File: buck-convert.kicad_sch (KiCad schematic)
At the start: 11 parts, among them IC1 LMR36510FADDAR

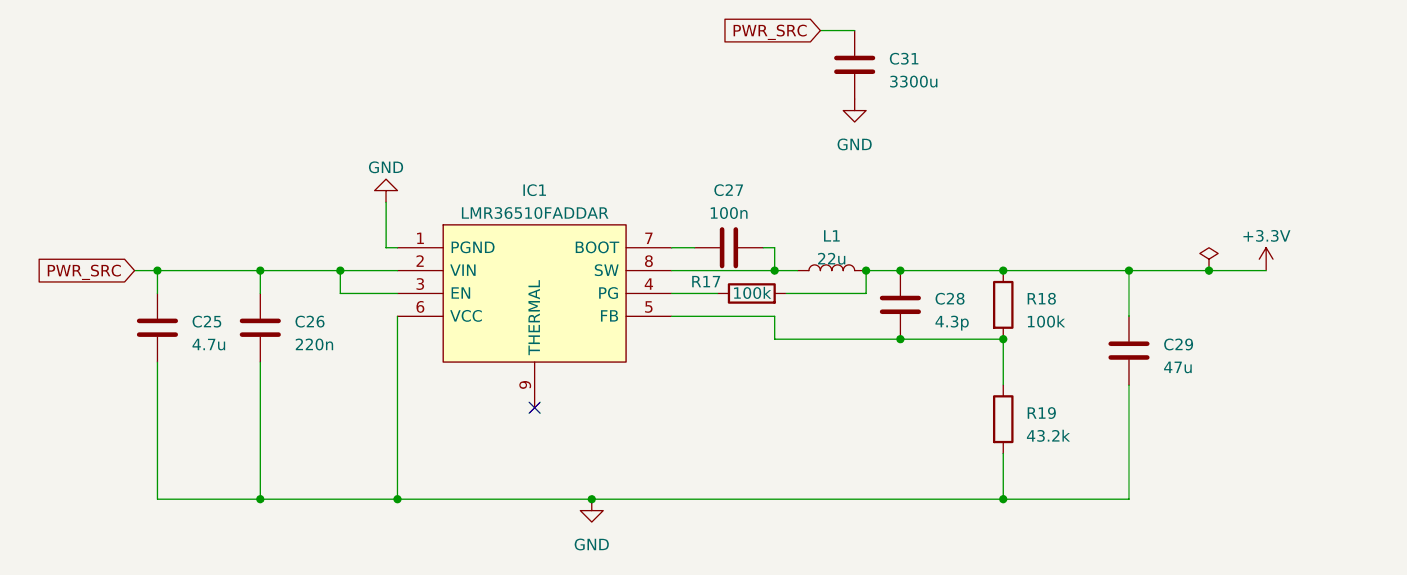
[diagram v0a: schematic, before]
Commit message: added nets to high level circuit
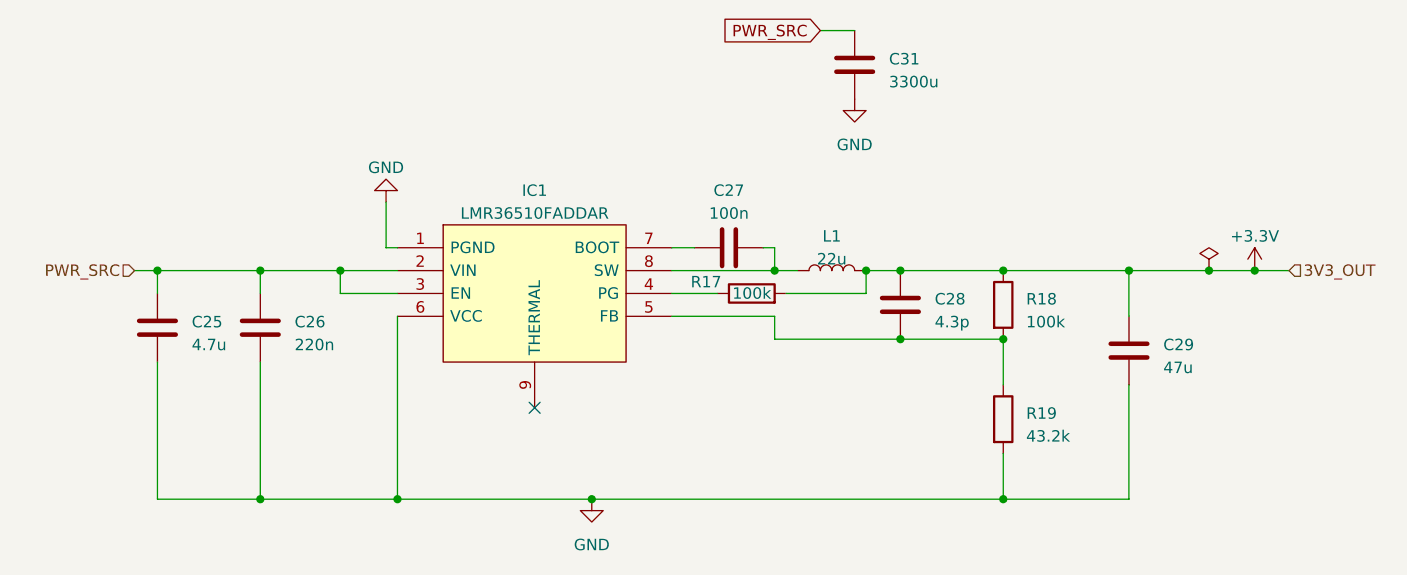
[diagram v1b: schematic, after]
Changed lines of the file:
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@@
   (junction (at 215.9 74.93) (diameter 0) (color 0 0 0 0)
+  )
+  (junction (at 229.87 74.93) (diameter 0) (color 0 0 0 0)
   )
   (no_connect (at 149.86 90.17))
@@
     (stroke (width 0) (type default))
   )
-  (wire (pts (xy 224.79 74.93) (xy 231.14 74.93))
+  (wire (pts (xy 224.79 74.93) (xy 229.87 74.93))
     (stroke (width 0) (type default))
   )
@@
     (stroke (width 0) (type default))
   )
+  (wire (pts (xy 229.87 74.93) (xy 233.68 74.93))
+    (stroke (width 0) (type default))
+  )
   (wire (pts (xy 107.95 100.33) (xy 119.38 100.33))
     (stroke (width 0) (type default))
@@
   (wire (pts (xy 181.61 48.26) (xy 185.42 48.26))
     (stroke (width 0) (type default))
-  )
-  (global_label "PWR_SRC" (shape input) (at 105.41 74.93 180) (fields_autoplaced)
-    (effects (font (size 1.27 1.27)) (justify right))
-    (property "Intersheetrefs" "${INTERSHEET_REFS}" (at 93.7957 74.93 0)
-      (effects (font (size 1.27 1.27)) (justify right) hide)
-    )
   )
   (global_label "PWR_SRC" (shape input) (at 181.61 48.26 180) (fields_autoplaced)
@@
       (effects (font (size 1.27 1.27)) (justify right) hide)
     )
+  )
+  (hierarchical_label "PWR_SRC" (shape input) (at 105.41 74.93 180) (fields_autoplaced)
+    (effects (font (size 1.27 1.27)) (justify right))
+  )
+  (hierarchical_label "3V3_OUT" (shape input) (at 233.68 74.93 0) (fields_autoplaced)
+    (effects (font (size 1.27 1.27)) (justify left))
   )
   (symbol (lib_id "Device:C") (at 119.38 81.28 0) (unit 1)
@@
   (symbol (lib_id "power:GND") (at 133.35 67.31 180) (unit 1)
     (in_bom yes) (on_board yes) (dnp no) (fields_autoplaced)
-    (property "Reference" "#PWR038" (at 133.35 60.96 0)
+    (property "Reference" "#PWR0102" (at 133.35 60.96 0)
       (effects (font (size 1.27 1.27)) hide)
     )
@@
       (project "electrium-esc-v2"
         (path "/be00c12c-11fa-42cb-8a0b-46fcd24b2ced/dedba472-5e9c-489a-b80e-963af35f7eb6"
-          (reference "#PWR038") (unit 1)
+          (reference "#PWR0102") (unit 1)
         )
       )
@@
   (symbol (lib_id "power:GND") (at 156.21 100.33 0) (unit 1)
     (in_bom yes) (on_board yes) (dnp no) (fields_autoplaced)
-    (property "Reference" "#PWR039" (at 156.21 106.68 0)
+    (property "Reference" "#PWR0101" (at 156.21 106.68 0)
       (effects (font (size 1.27 1.27)) hide)
     )
@@
       (project "electrium-esc-v2"
         (path "/be00c12c-11fa-42cb-8a0b-46fcd24b2ced/dedba472-5e9c-489a-b80e-963af35f7eb6"
-          (reference "#PWR039") (unit 1)
+          (reference "#PWR0101") (unit 1)
         )
       )
@@
     )
   )
-  (symbol (lib_id "power:+3.3V") (at 231.14 74.93 0) (unit 1)
-    (in_bom yes) (on_board yes) (dnp no) (fields_autoplaced)
-    (property "Reference" "#PWR040" (at 231.14 78.74 0)
-      (effects (font (size 1.27 1.27)) hide)
-    )
-    (property "Value" "+3.3V" (at 231.14 71.12 0)
-      (effects (font (size 1.27 1.27)))
-    )
-    (property "Footprint" "" (at 231.14 74.93 0)
-      (effects (font (size 1.27 1.27)) hide)
-    )
-    (property "Datasheet" "" (at 231.14 74.93 0)
-      (effects (font (size 1.27 1.27)) hide)
-    )
-    (pin "1")
-    (instances
-      (project "electrium-esc-v2"
-        (path "/be00c12c-11fa-42cb-8a0b-46fcd24b2ced/dedba472-5e9c-489a-b80e-963af35f7eb6"
-          (reference "#PWR040") (unit 1)
+  (symbol (lib_id "power:+3.3V") (at 229.87 74.93 0) (unit 1)
+    (in_bom yes) (on_board yes) (dnp no) (fields_autoplaced)
+    (property "Reference" "#PWR0104" (at 229.87 78.74 0)
+      (effects (font (size 1.27 1.27)) hide)
+    )
+    (property "Value" "+3.3V" (at 229.87 71.12 0)
+      (effects (font (size 1.27 1.27)))
+    )
+    (property "Footprint" "" (at 229.87 74.93 0)
+      (effects (font (size 1.27 1.27)) hide)
+    )
+    (property "Datasheet" "" (at 229.87 74.93 0)
+      (effects (font (size 1.27 1.27)) hide)
+    )
+    (pin "1")
+    (instances
+      (project "electrium-esc-v2"
+        (path "/be00c12c-11fa-42cb-8a0b-46fcd24b2ced/dedba472-5e9c-489a-b80e-963af35f7eb6"
+          (reference "#PWR0104") (unit 1)
         )
       )
@@
   (symbol (lib_id "power:GND") (at 185.42 55.88 0) (unit 1)
     (in_bom yes) (on_board yes) (dnp no) (fields_autoplaced)
-    (property "Reference" "#PWR043" (at 185.42 62.23 0)
+    (property "Reference" "#PWR0103" (at 185.42 62.23 0)
       (effects (font (size 1.27 1.27)) hide)
     )
@@
       (project "electrium-esc-v2"
         (path "/be00c12c-11fa-42cb-8a0b-46fcd24b2ced/dedba472-5e9c-489a-b80e-963af35f7eb6"
-          (reference "#PWR043") (unit 1)
-        )
-      )
+          (reference "#PWR0103") (unit 1)
+        )
+      )
